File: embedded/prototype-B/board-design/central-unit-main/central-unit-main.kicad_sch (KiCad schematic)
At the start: 1 part, among them U1 ATMEGA328P-AUR

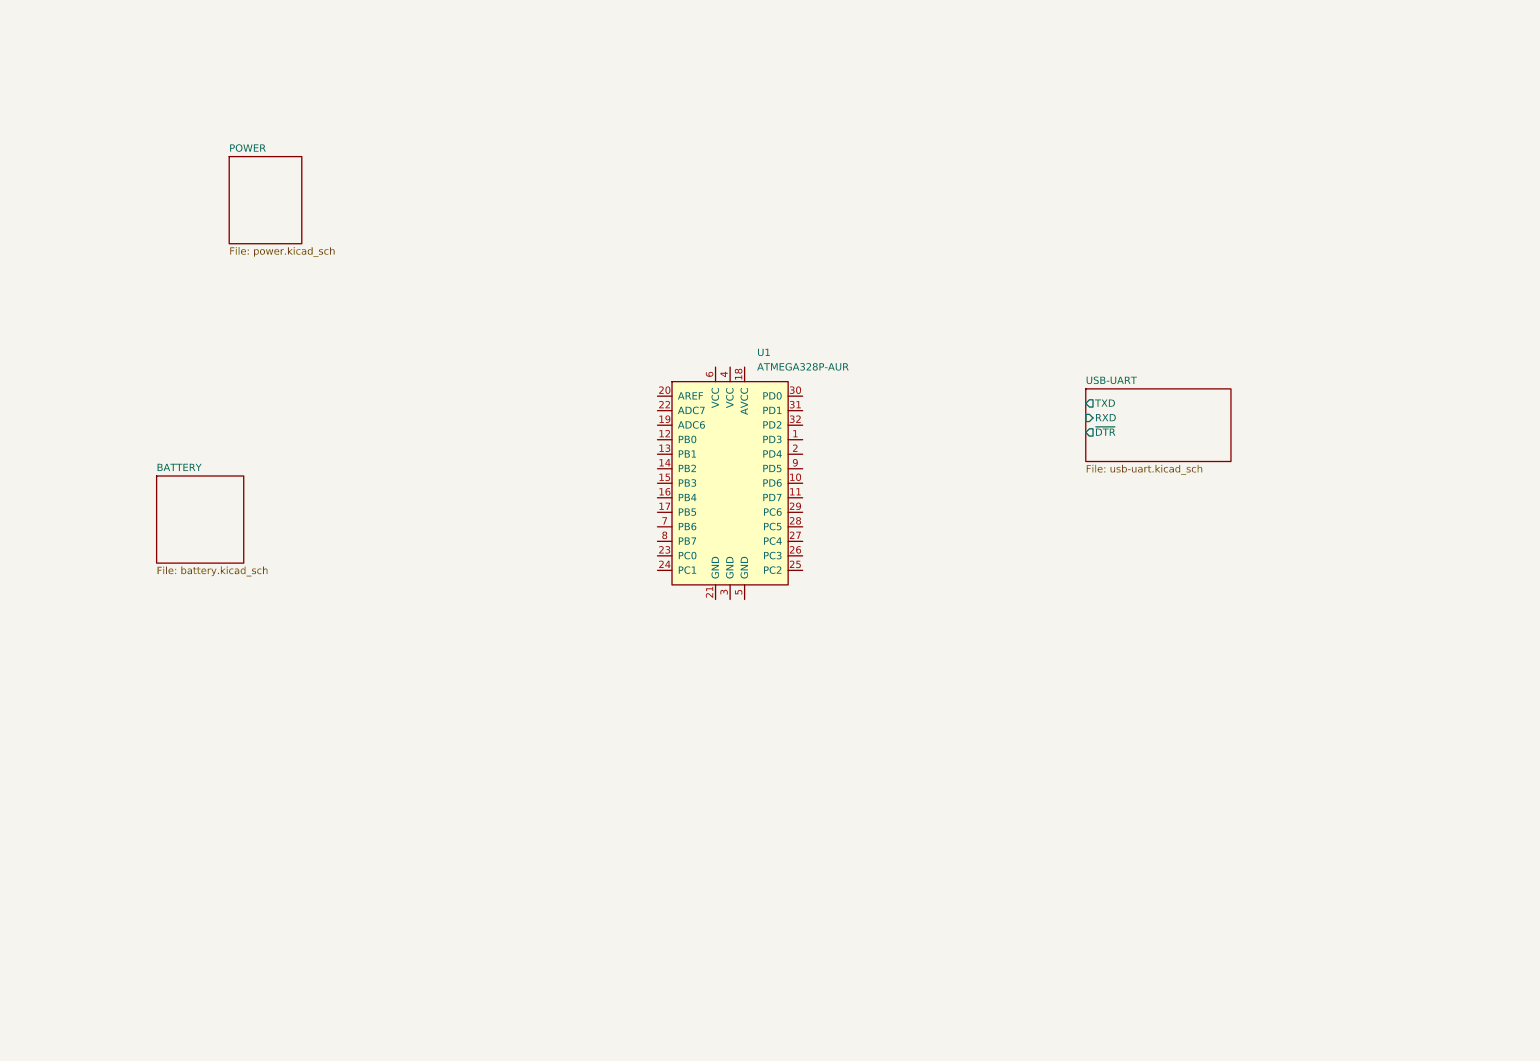
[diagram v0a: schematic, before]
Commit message: [Central Unit] Design USB connection
Schematic of the USB connection and boot considerations for STM32L452RE.

Signed-off-by: Nicolae-Andrei Vasile <vasilenicolaeandrei@gmail.com>
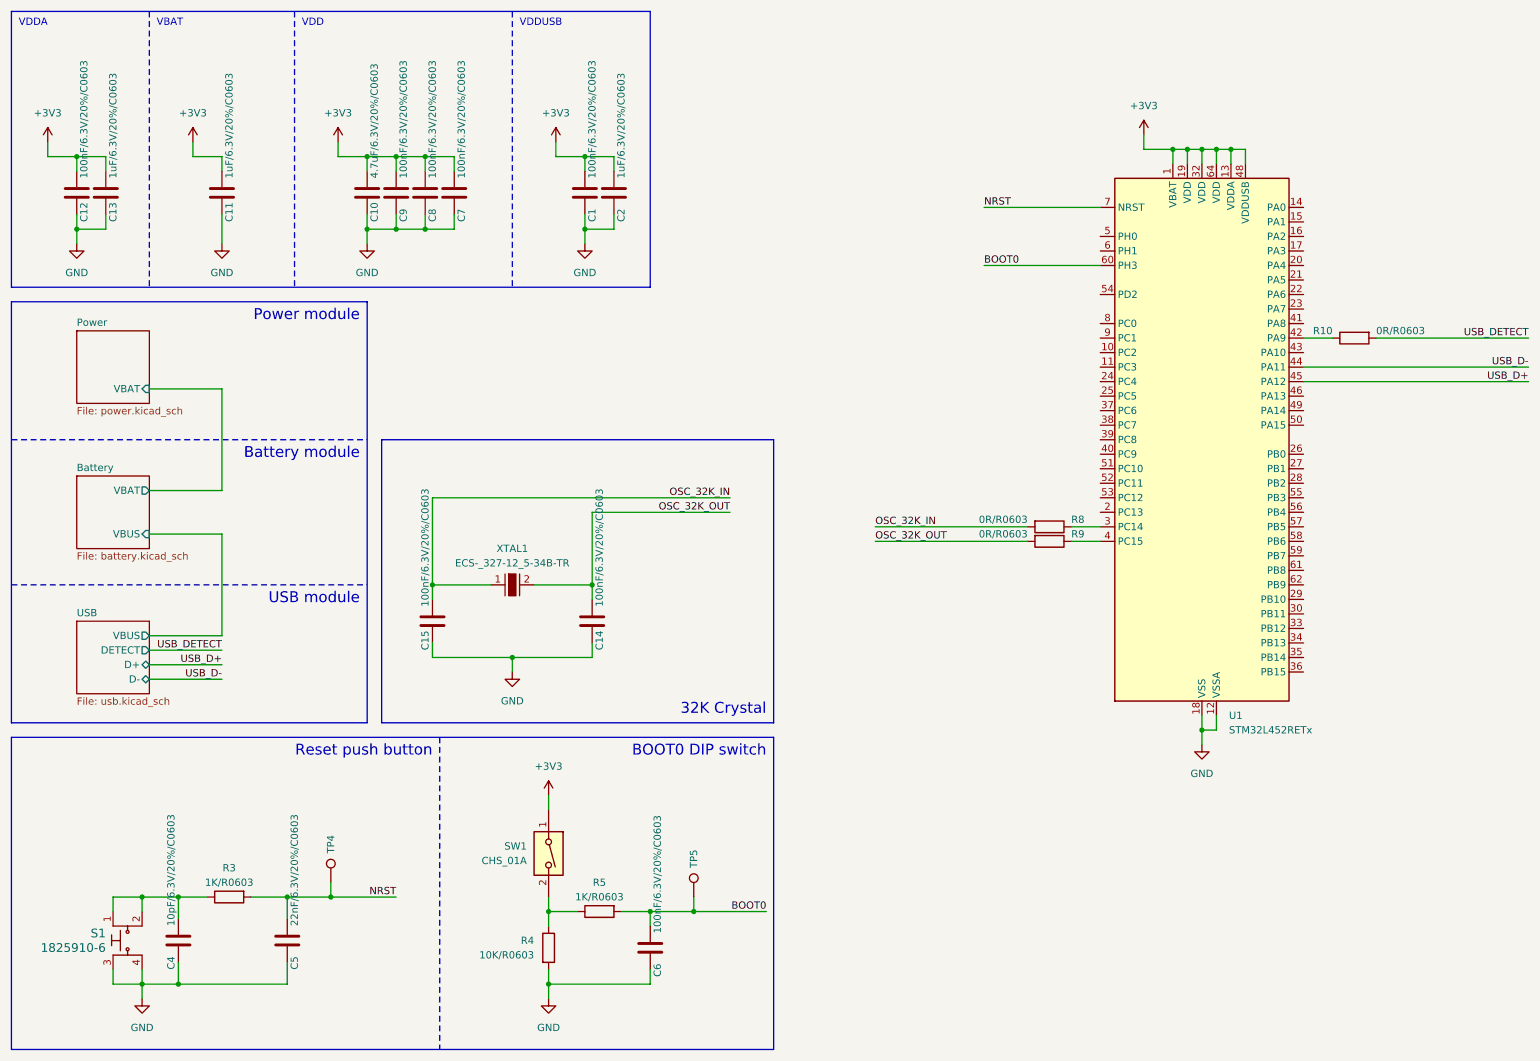
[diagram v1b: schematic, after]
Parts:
- removed U1: ATMEGA328P-AUR, digikey-footprints:TQFP-32_7x7mm, symbol dk_Embedded-Microcontrollers:ATMEGA328P-AUR
- added C1, C12, C14, C15, C6, C7, C8, C9: 100nF/6.3V/20%/C0603, Capacitor_SMD:C_0603_1608Metric_Pad1.08x0.95mm_HandSolder, symbol Device:C
- added C10: 4.7uF/6.3V/20%/C0603, Capacitor_SMD:C_0603_1608Metric_Pad1.08x0.95mm_HandSolder, symbol Device:C
- added C11, C13, C2: 1uF/6.3V/20%/C0603, Capacitor_SMD:C_0603_1608Metric_Pad1.08x0.95mm_HandSolder, symbol Device:C
- added C4: 10pF/6.3V/20%/C0603, Capacitor_SMD:C_0603_1608Metric_Pad1.08x0.95mm_HandSolder, symbol Device:C
- added C5: 22nF/6.3V/20%/C0603, Capacitor_SMD:C_0603_1608Metric_Pad1.08x0.95mm_HandSolder, symbol Device:C
- added R10, R8, R9: 0R/R0603, Resistor_SMD:R_0603_1608Metric_Pad0.98x0.95mm_HandSolder, symbol Device:R
- added R3, R5: 1K/R0603, Resistor_SMD:R_0603_1608Metric_Pad0.98x0.95mm_HandSolder, symbol Device:R
- added R4: 10K/R0603, Resistor_SMD:R_0603_1608Metric_Pad0.98x0.95mm_HandSolder, symbol Device:R
- added S1: 1825910-6, digikey-footprints:Switch_Tactile_THT_6x6mm, symbol dk_Tactile-Switches:1825910-6
- added SW1: CHS_01A, Button_Switch_SMD:SW_DIP_SPSTx01_Slide_Copal_CHS-01A_W5.08mm_P1.27mm_JPin, symbol Switch:SW_DIP_x01
- added TP4, TP5: TestPoint, symbol Connector:TestPoint
- added U1: STM32L452RETx, Package_QFP:LQFP-64_10x10mm_P0.5mm, symbol MCU_ST_STM32L4:STM32L452RETx
- added XTAL1: ECS-_327-12_5-34B-TR, digikey-footprints:SMD-2_3.2x1.5mm, symbol dk_Crystals:ECS-_327-12_5-34B-TR
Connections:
- new net: R4.1, R5.1, SW1.2
- new net: R9.1, U1.4 (PC15)
- new net: R8.1, U1.3 (PC14)
- new net: C4.1, R3.1, S1.1, S1.2
- new net: R10.1, U1.42 (PA9)
- new net +3V3: C1.1, C10.1, C11.1, C12.1, C13.1, C2.1, C7.1, C8.1, C9.1, SW1.1, U1.1 (VBAT), U1.13 (VDDA), U1.19 (VDD), U1.32 (VDD), U1.48 (VDDUSB), U1.64 (VDD)
- new net BOOT0: C6.1, R5.2, TP5.1, U1.60 (PH3)
- new net GND: C1.2, C10.2, C11.2, C12.2, C13.2, C14.2, C15.2, C2.2, C4.2, C5.2, C6.2, C7.2, C8.2, C9.2, R4.2, S1.3, S1.4, U1.12 (VSSA), U1.18 (VSS), U1.31 (VSS), U1.47 (VSS), U1.63 (VSS)
- new net NRST: C5.1, R3.2, TP4.1, U1.7 (NRST)
- new net OSC_32K_IN: C15.1, R8.2, XTAL1.1
- new net OSC_32K_OUT: C14.1, R9.2, XTAL1.2
- new net USB_D+: U1.45 (PA12)
- new net USB_D-: U1.44 (PA11)
- new net USB_DETECT: R10.2
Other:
- removed sheet BATTERY
- removed sheet POWER
- removed sheet USB-UART
- added sheet Battery (battery.kicad_sch)
- added sheet Power (power.kicad_sch)
- added sheet USB (usb.kicad_sch)
- note added: "32K Crystal"
- note added: "BOOT0 DIP switch"
- note added: "Battery module"
- note added: "Power module"
- note added: "Reset push button"
- note added: "USB module"
- note added: "VBAT"
- note added: "VDD"
- note added: "VDDA"
- note added: "VDDUSB"

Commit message: [Central unit] Power domain
Documented and implemented a first version of the main power domain for
the device.

Signed-off-by: Nicolae-Andrei Vasile <vasilenicolaeandrei@gmail.com>
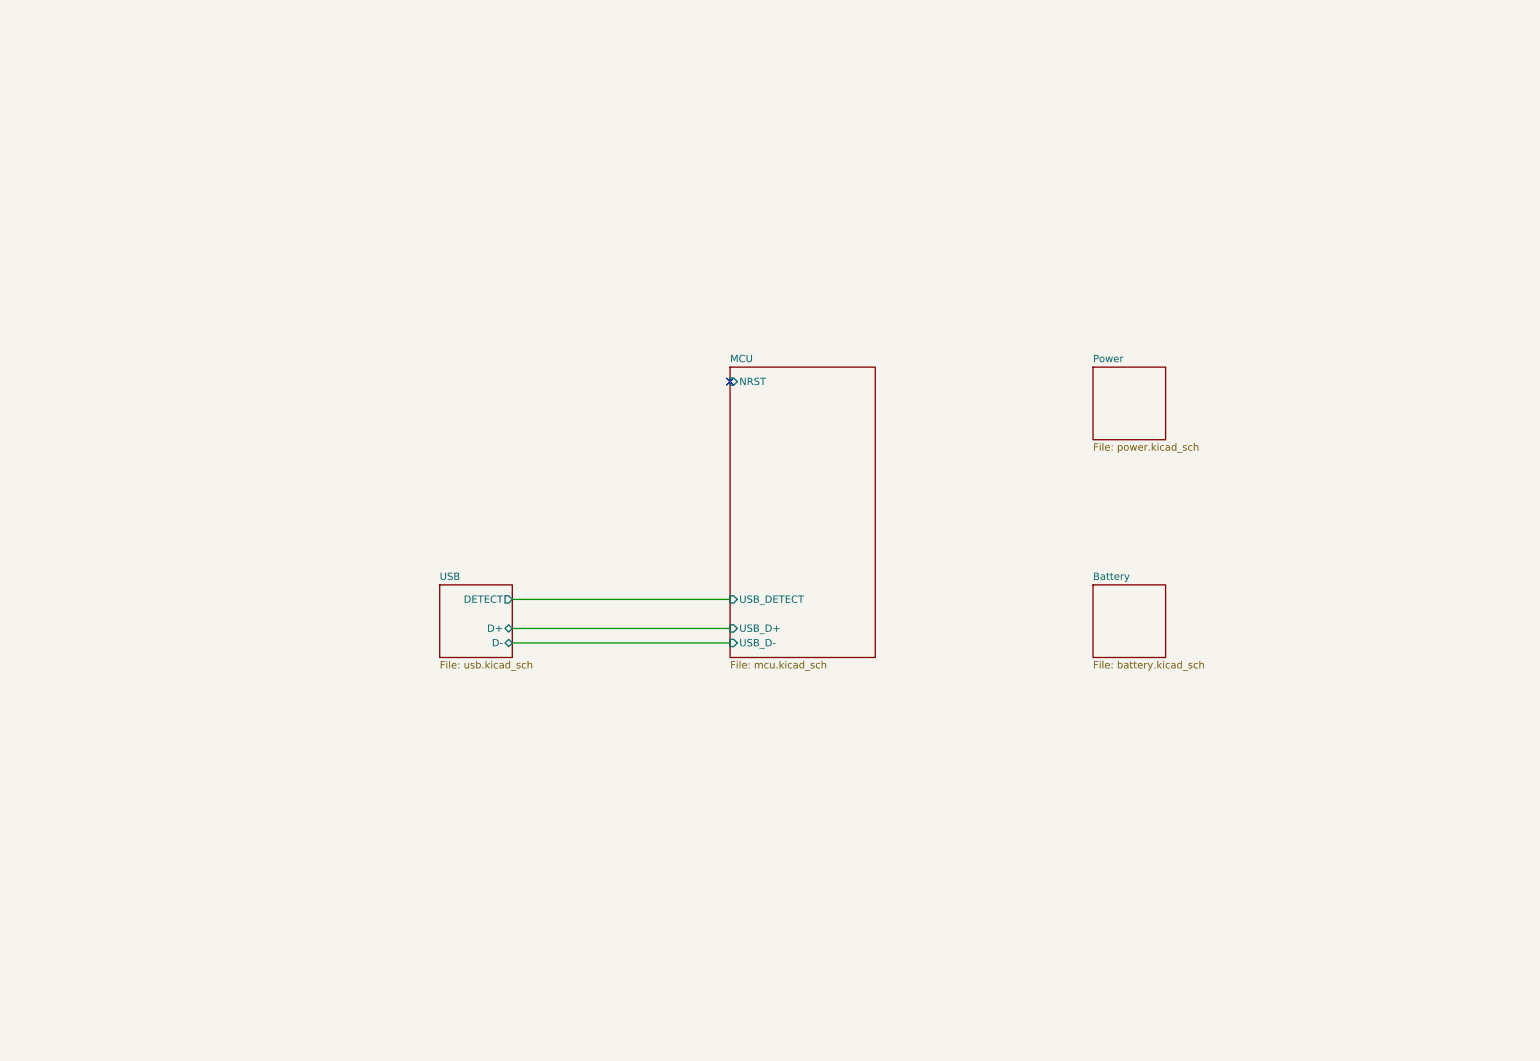
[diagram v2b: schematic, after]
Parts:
- removed C1, C12, C14, C15, C6, C7, C8, C9: 100nF/6.3V/20%/C0603, Capacitor_SMD:C_0603_1608Metric_Pad1.08x0.95mm_HandSolder, symbol Device:C
- removed C10: 4.7uF/6.3V/20%/C0603, Capacitor_SMD:C_0603_1608Metric_Pad1.08x0.95mm_HandSolder, symbol Device:C
- removed C11, C13, C2: 1uF/6.3V/20%/C0603, Capacitor_SMD:C_0603_1608Metric_Pad1.08x0.95mm_HandSolder, symbol Device:C
- removed C4: 10pF/6.3V/20%/C0603, Capacitor_SMD:C_0603_1608Metric_Pad1.08x0.95mm_HandSolder, symbol Device:C
- removed C5: 22nF/6.3V/20%/C0603, Capacitor_SMD:C_0603_1608Metric_Pad1.08x0.95mm_HandSolder, symbol Device:C
- removed R10, R8, R9: 0R/R0603, Resistor_SMD:R_0603_1608Metric_Pad0.98x0.95mm_HandSolder, symbol Device:R
- removed R3, R5: 1K/R0603, Resistor_SMD:R_0603_1608Metric_Pad0.98x0.95mm_HandSolder, symbol Device:R
- removed R4: 10K/R0603, Resistor_SMD:R_0603_1608Metric_Pad0.98x0.95mm_HandSolder, symbol Device:R
- removed S1: 1825910-6, digikey-footprints:Switch_Tactile_THT_6x6mm, symbol dk_Tactile-Switches:1825910-6
- removed SW1: CHS_01A, Button_Switch_SMD:SW_DIP_SPSTx01_Slide_Copal_CHS-01A_W5.08mm_P1.27mm_JPin, symbol Switch:SW_DIP_x01
- removed TP4, TP5: TestPoint, symbol Connector:TestPoint
- removed U1: STM32L452RETx, Package_QFP:LQFP-64_10x10mm_P0.5mm, symbol MCU_ST_STM32L4:STM32L452RETx
- removed XTAL1: ECS-_327-12_5-34B-TR, digikey-footprints:SMD-2_3.2x1.5mm, symbol dk_Crystals:ECS-_327-12_5-34B-TR
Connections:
- no-connect marks 0 -> 1
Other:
- added sheet MCU (mcu.kicad_sch)
- sheet Battery ports: added none; removed VBAT, VBUS
- sheet Power ports: added none; removed VBAT
- sheet USB ports: added none; removed VBUS
- note removed: "32K Crystal"
- note removed: "BOOT0 DIP switch"
- note removed: "Battery module"
- note removed: "Power module"
- note removed: "Reset push button"
- note removed: "USB module"
- note removed: "VBAT"
- note removed: "VDD"
- note removed: "VDDA"
- note removed: "VDDUSB"

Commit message: [Central unit] Battery charger
Added battery charging circuit to the schematic. Refactored BOOT0 logic
and included an entry for the external push button to power ON/OFF the device.

Signed-off-by: Nicolae-Andrei Vasile <vasilenicolaeandrei@gmail.com>
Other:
- title: (none) -> Retrolight
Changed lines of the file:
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@@
 	(paper "A4")
 	(title_block
-		(date "2026-04-06")
+		(title "Retrolight")
+		(date "2026-04-14")
+		(rev "B")
 	)
 	(no_connect

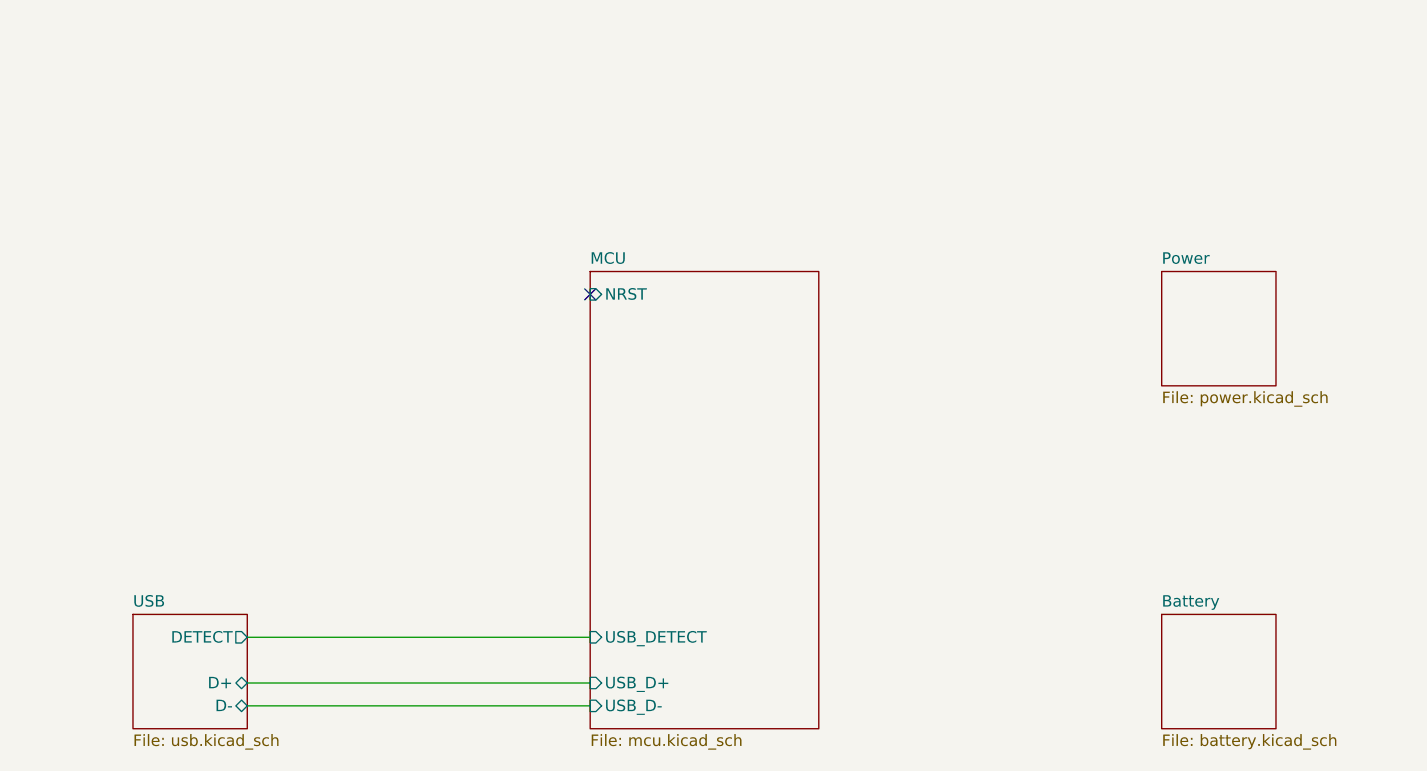
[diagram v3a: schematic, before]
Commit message: [Central unit] Sensors
Added an ambient light sensor for nighttime detection and an
accelerometer for monitoring the movement patterns of the device.

Signed-off-by: Nicolae-Andrei Vasile <vasilenicolaeandrei@gmail.com>
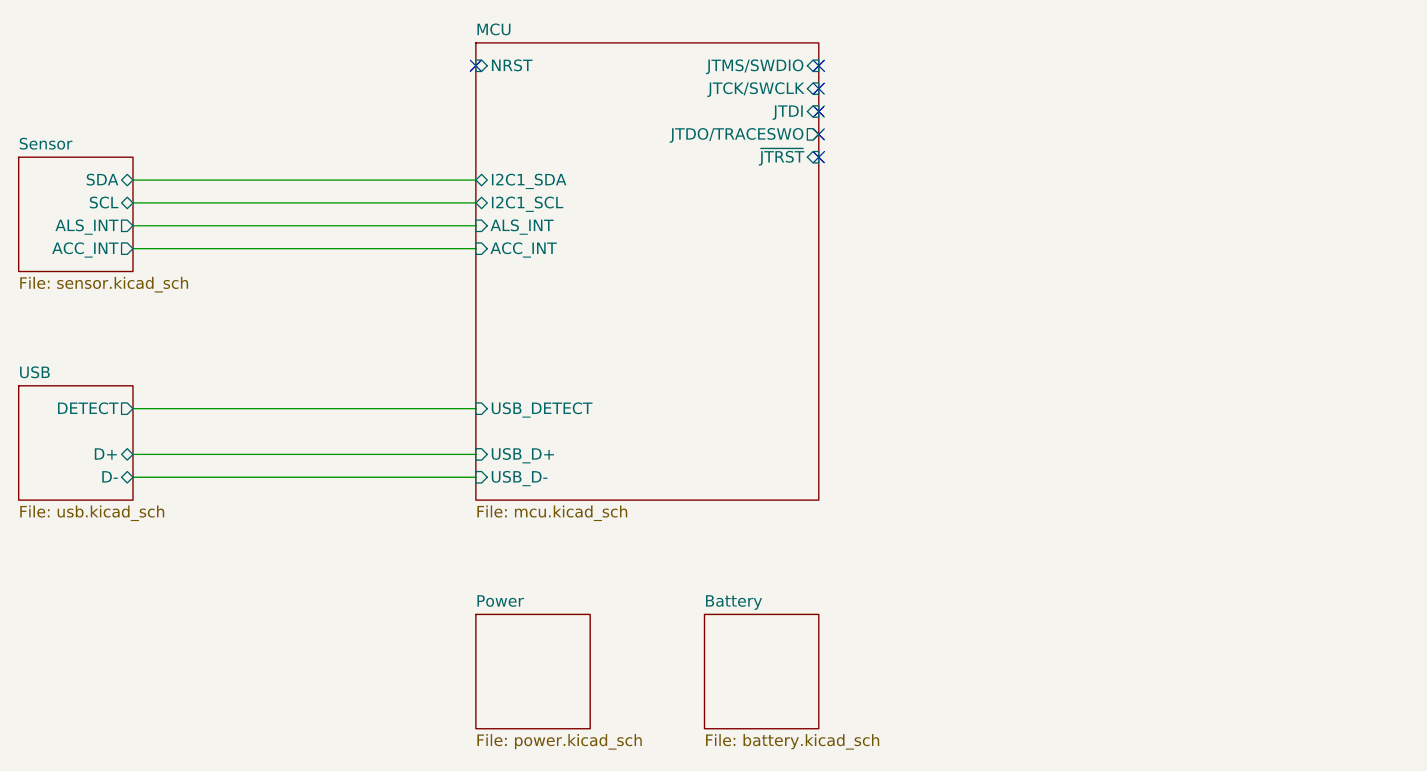
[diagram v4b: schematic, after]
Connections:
- no-connect marks 1 -> 6
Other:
- added sheet Sensor (sensor.kicad_sch)
- sheet MCU ports: added ACC_INT, ALS_INT, I2C1_SCL, I2C1_SDA, JTCK/SWCLK, JTDI, JTDO/TRACESWO, JTMS/SWDIO, ~{JTRST}; removed none
